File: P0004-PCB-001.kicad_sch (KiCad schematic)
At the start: 5 parts

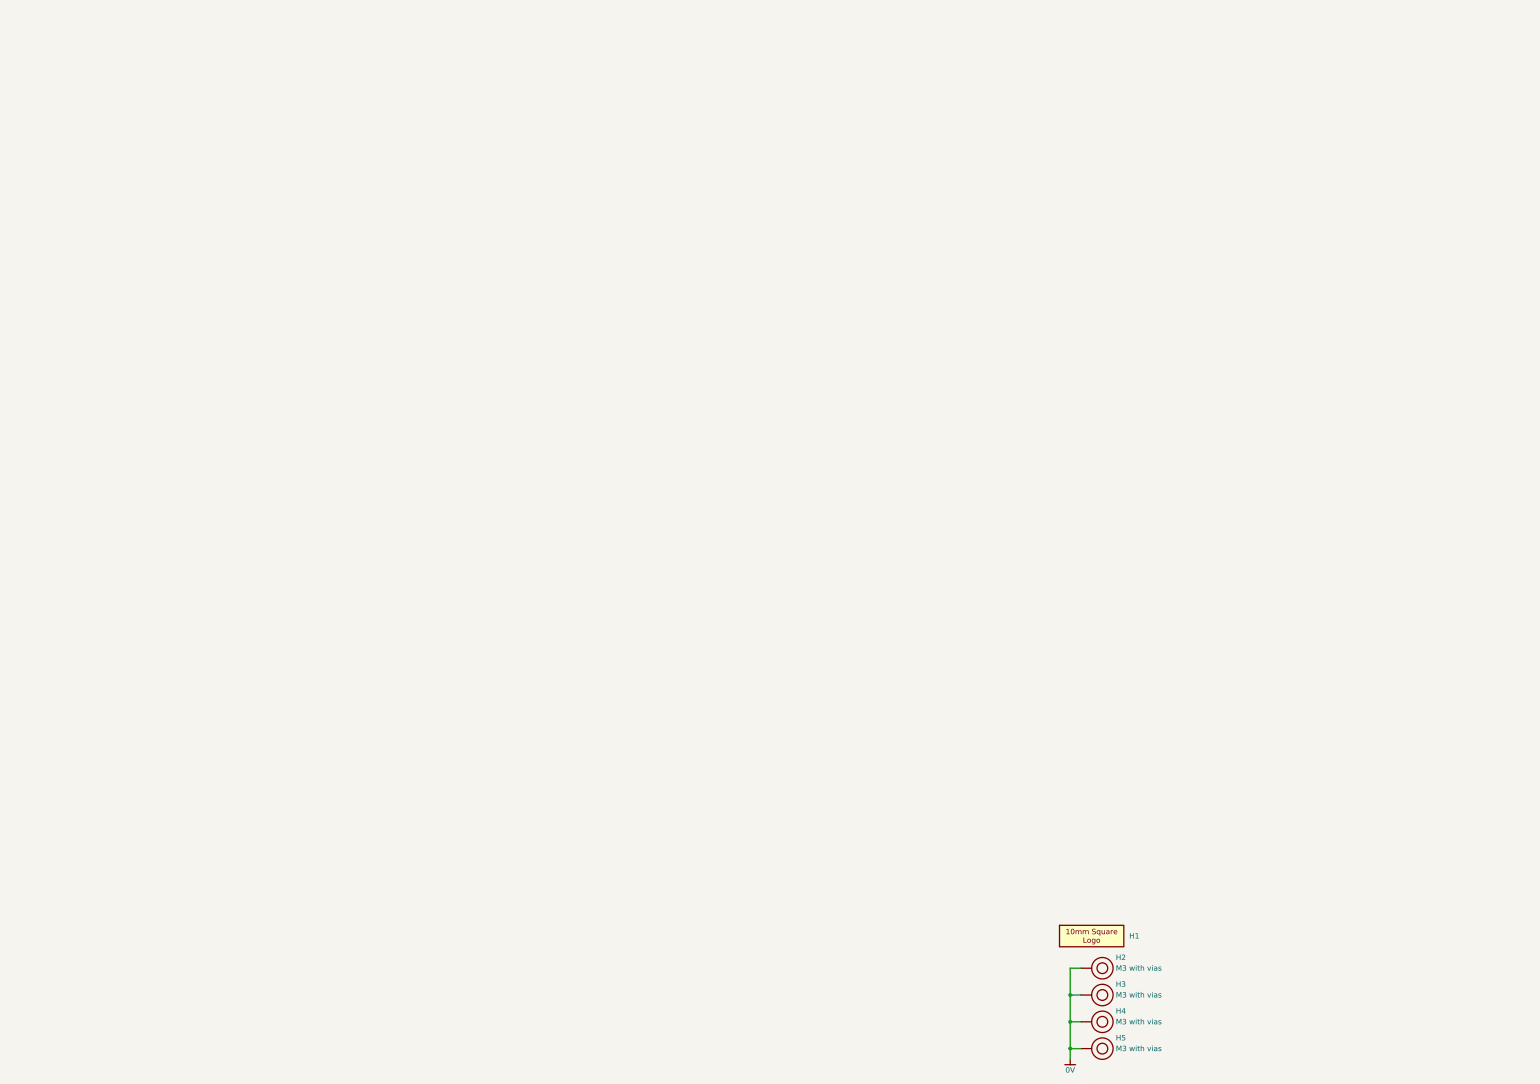
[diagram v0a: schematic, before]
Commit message: started adding components
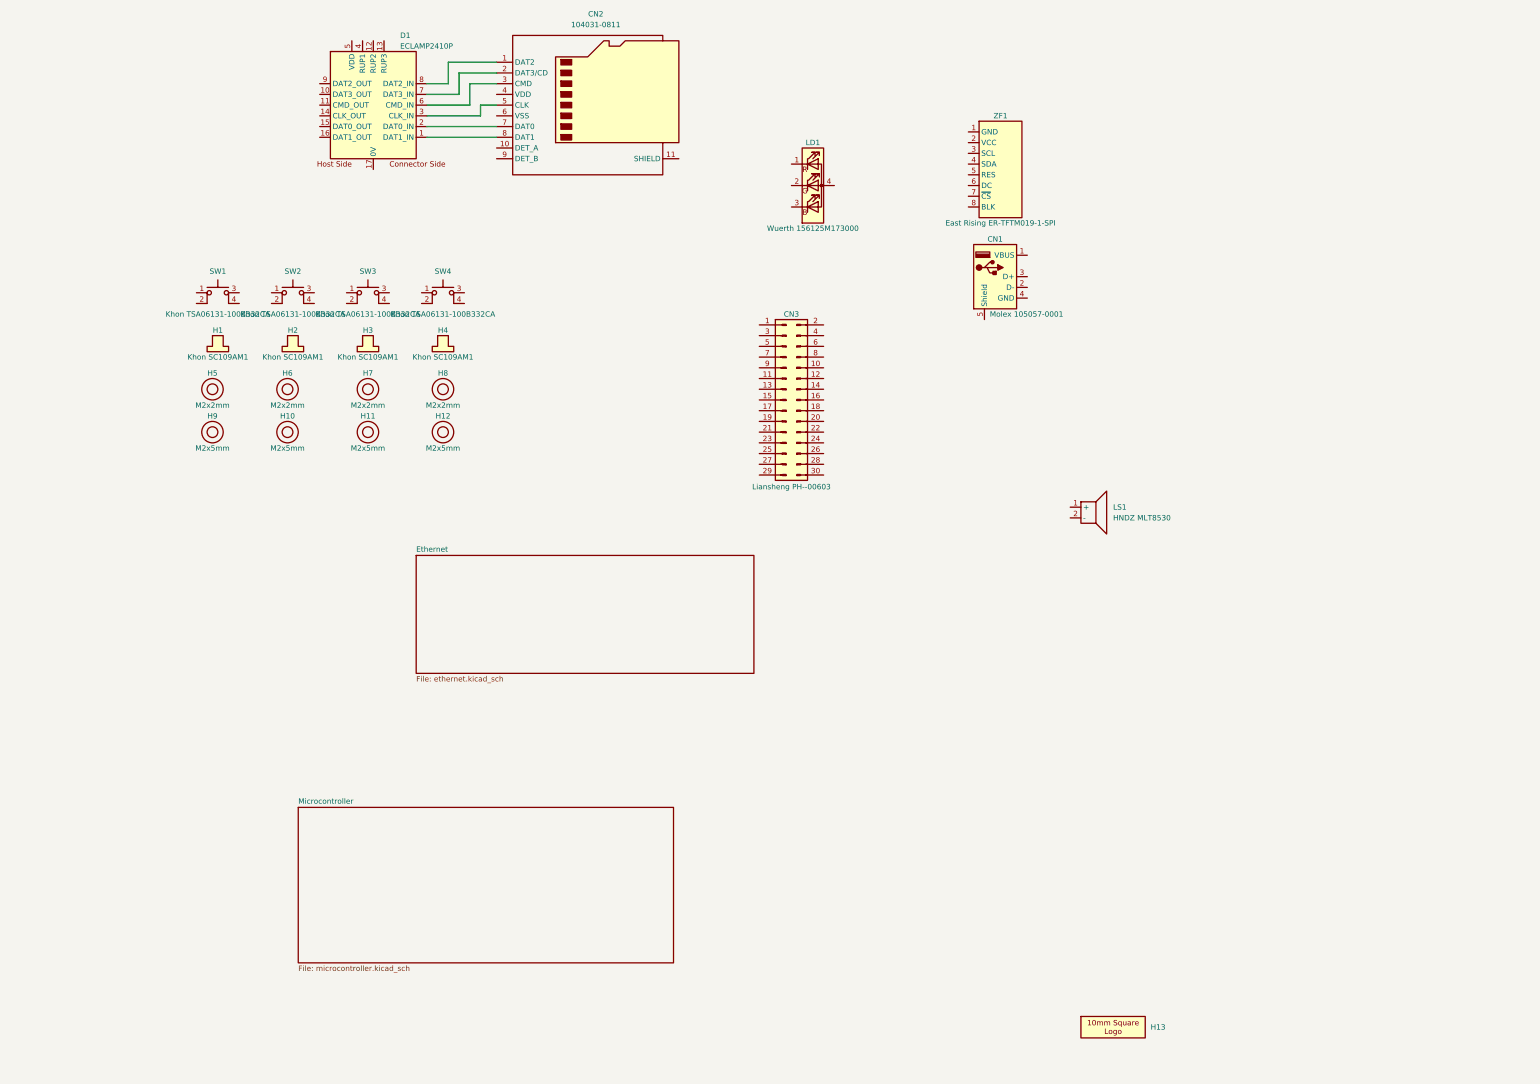
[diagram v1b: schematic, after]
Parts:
- removed H1: (no value), Misc_WUT:Logo_10mmx10mm, symbol Layout_WUT:Logo_10mmx10mm
- removed H2, H3, H4, H5: M3 with vias, MountingHole:MountingHole_3.2mm_M3_Pad_Via, symbol Layout_WUT:M3_with_Vias
- added CN1: Molex 105057-0001, Connector_WUT:USB-A_Molex_105057-0001_TH_Vertical, symbol Connector_WUT:Molex_105057-0001
- added CN2: 104031-0811, Connector_WUT:microSD_HC_Molex_104031-0811, symbol Connector_WUT:Molex_104031-0811
- added CN3: Liansheng PH--00603, Connector_WUT:Liansheng_PH--00603, symbol Connector_WUT:Liansheng_PH-00603
- added D1: ECLAMP2410P, Diode_WUT:Semtech_ECLAMP2410P, symbol Diode_WUT:Semtech_EClamp2410P
- added H1, H2, H3, H4: Khon SC109AM1, Switch_WUT:Khon_SC109, symbol Switch_WUT:Khon_SC109AM1
- added H10, H11, H12, H9: M2x5mm, Accessories_WUT:Accu_HPS-4-2.2-5-POM-BL, symbol Accessories_WUT:Accu_HPS-4-2.2-5-POM-BL
- added H13: (no value), Misc_WUT:Logo_10mmx10mm, symbol Layout_WUT:Logo_10mmx10mm
- added H5, H6, H7, H8: M2x2mm, Accessories_WUT:Accu_HPS-4-2.2-2-POM-BL, symbol Accessories_WUT:Accu_HPS-4-2.2-2-POM-BL
- added LD1: Wuerth 156125M173000, LED_WUT:Wuerth_156125M173000, symbol LED_WUT:Wuerth_156125M173000
- added LS1: HNDZ MLT8530, Audio_WUT:HNDZ_MLT8530, symbol Audio_WUT:HNDZ_MLT8530
- added SW1, SW2, SW3, SW4: Khon TSA06131-100B332CA, Switch_WUT:Khon_TSB06331-090, symbol Switch_WUT:Khon_TSB06331-090D332DA-R0500
- added ZF1: East Rising ER-TFTM019-1-SPI, Display_WUT:East-Rising_ER-TFTM019-1-SPI, symbol Display_WUT:East-Rising_ER-TFTM019-1-SPI
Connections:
- new net: LS1.3, LS1.4
- new net: CN2.8 (DAT1), D1.1 (DAT1_IN)
- new net: CN2.7 (DAT0), D1.2 (DAT0_IN)
- new net: CN2.5 (CLK), D1.3 (CLK_IN)
- new net: CN2.3 (CMD), D1.6 (CMD_IN)
- new net: CN2.2 (DAT3/CD), D1.7 (DAT3_IN)
- new net: CN2.1 (DAT2), D1.8 (DAT2_IN)
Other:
- added sheet Ethernet (ethernet.kicad_sch)
- added sheet Microcontroller (microcontroller.kicad_sch)

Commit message: testing ci config
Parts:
- SW1, SW2, SW3, SW4: value Khon TSA06131-100B332CA -> Khon TSB06331-090D332DA-R0500
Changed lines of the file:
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@@
 		(fields_autoplaced yes)
 		(property "Reference" "SW2"
+			(at 78.74 88.9 0)
+			(show_name no)
+			(do_not_autoplace no)
+			(effects
+				(font
+					(size 1.27 1.27)
+				)
+			)
+		)
+		(property "Value" "Khon TSB06331-090D332DA-R0500"
 			(at 78.74 91.44 0)
 			(show_name no)
 			(do_not_autoplace no)
-			(effects
-				(font
-					(size 1.27 1.27)
-				)
-			)
-		)
-		(property "Value" "Khon TSA06131-100B332CA"
-			(at 78.74 101.6 0)
-			(show_name no)
-			(do_not_autoplace yes)
 			(effects
 				(font
@@
 		(fields_autoplaced yes)
 		(property "Reference" "SW4"
+			(at 114.3 88.9 0)
+			(show_name no)
+			(do_not_autoplace no)
+			(effects
+				(font
+					(size 1.27 1.27)
+				)
+			)
+		)
+		(property "Value" "Khon TSB06331-090D332DA-R0500"
 			(at 114.3 91.44 0)
 			(show_name no)
 			(do_not_autoplace no)
-			(effects
-				(font
-					(size 1.27 1.27)
-				)
-			)
-		)
-		(property "Value" "Khon TSA06131-100B332CA"
-			(at 114.3 101.6 0)
-			(show_name no)
-			(do_not_autoplace yes)
 			(effects
 				(font
@@
 		(in_bom yes)
 		(on_board yes)
-		(in_pos_files yes)
+		(in_pos_files no)
 		(dnp no)
 		(fields_autoplaced yes)
@@
 		(in_bom yes)
 		(on_board yes)
-		(in_pos_files yes)
+		(in_pos_files no)
 		(dnp no)
 		(fields_autoplaced yes)
@@
 		(fields_autoplaced yes)
 		(property "Reference" "SW1"
+			(at 60.96 88.9 0)
+			(show_name no)
+			(do_not_autoplace no)
+			(effects
+				(font
+					(size 1.27 1.27)
+				)
+			)
+		)
+		(property "Value" "Khon TSB06331-090D332DA-R0500"
 			(at 60.96 91.44 0)
 			(show_name no)
 			(do_not_autoplace no)
-			(effects
-				(font
-					(size 1.27 1.27)
-				)
-			)
-		)
-		(property "Value" "Khon TSA06131-100B332CA"
-			(at 60.96 101.6 0)
-			(show_name no)
-			(do_not_autoplace yes)
 			(effects
 				(font
@@
 		(in_bom yes)
 		(on_board yes)
-		(in_pos_files yes)
+		(in_pos_files no)
 		(dnp no)
 		(fields_autoplaced yes)
@@
 		(fields_autoplaced yes)
 		(property "Reference" "SW3"
+			(at 96.52 88.9 0)
+			(show_name no)
+			(do_not_autoplace no)
+			(effects
+				(font
+					(size 1.27 1.27)
+				)
+			)
+		)
+		(property "Value" "Khon TSB06331-090D332DA-R0500"
 			(at 96.52 91.44 0)
 			(show_name no)
 			(do_not_autoplace no)
-			(effects
-				(font
-					(size 1.27 1.27)
-				)
-			)
-		)
-		(property "Value" "Khon TSA06131-100B332CA"
-			(at 96.52 101.6 0)
-			(show_name no)
-			(do_not_autoplace yes)
 			(effects
 				(font
@@
 		(in_bom yes)
 		(on_board yes)
-		(in_pos_files yes)
+		(in_pos_files no)
 		(dnp no)
 		(fields_autoplaced yes)

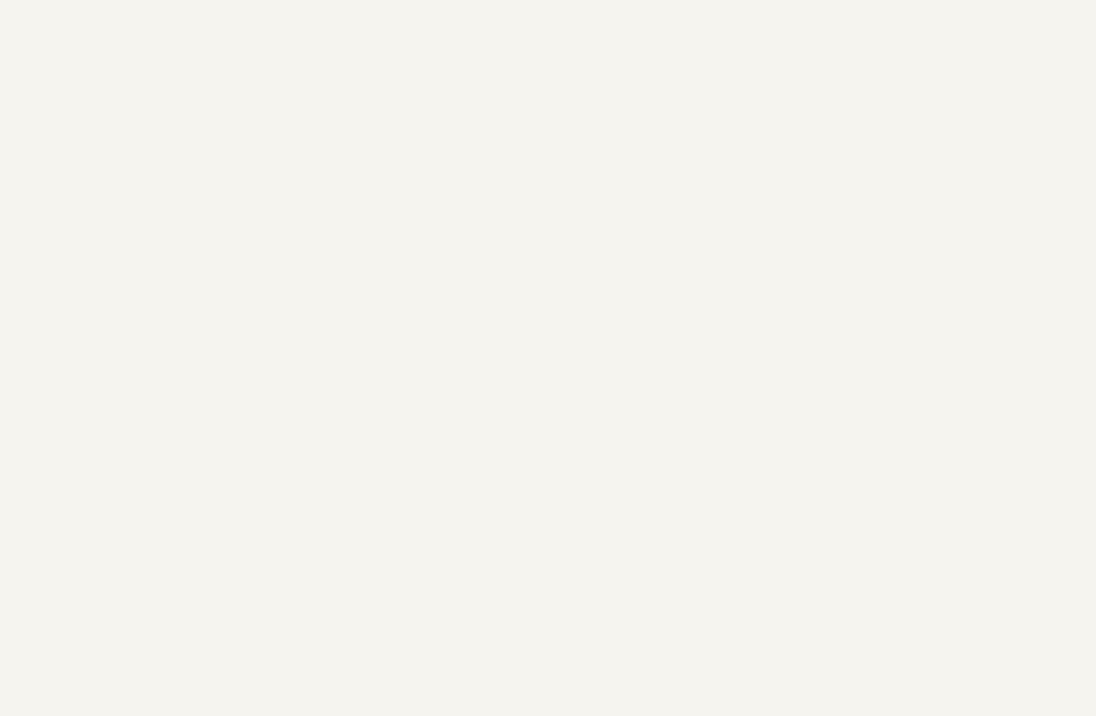
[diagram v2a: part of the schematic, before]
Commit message: started on DCDC section
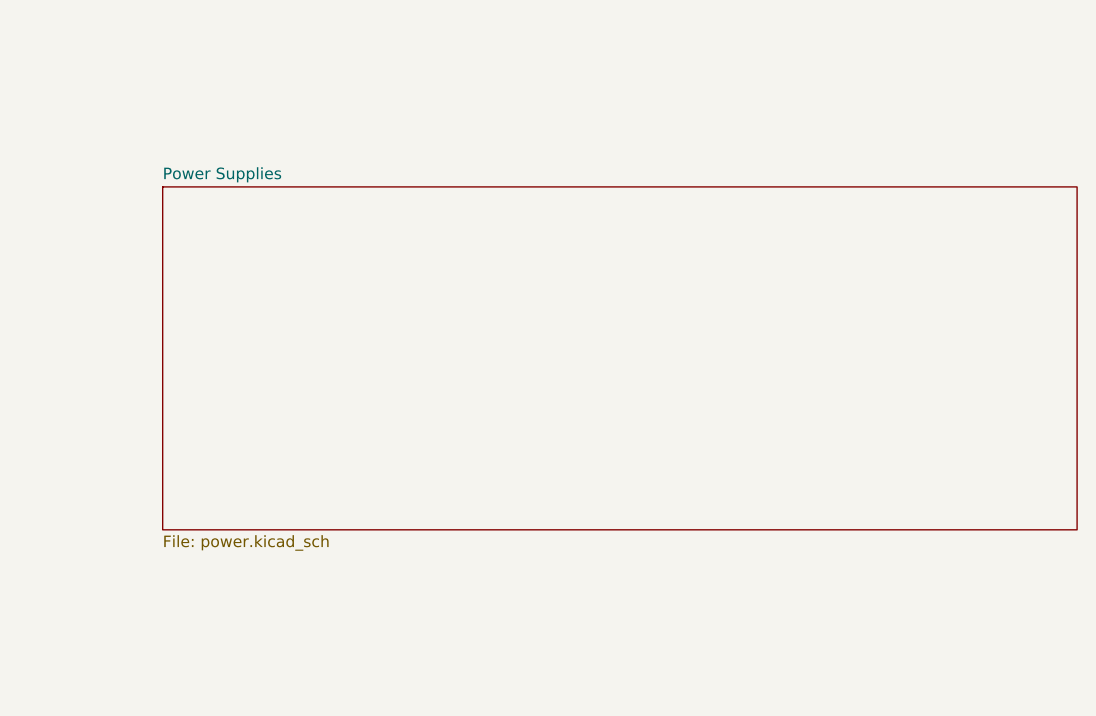
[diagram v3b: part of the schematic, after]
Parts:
- H1, H2, H3, H4: JLCPCB Order # (none) -> C42435457; MPN (none) -> SC109AM1; Manufacturer (none) -> Khon
- LD1: JLCPCB Order # (none) -> C5341671; MPN https://www.we-online.com/components/products/datasheet/156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 -> 156125M173000
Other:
- added sheet Power Supplies (power.kicad_sch)
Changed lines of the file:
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@@
 			)
 		)
-		(property "Datasheet" ""
+		(property "Datasheet" "https://www.khon-switch.com/upload/1c/202307/SC109%20Switch%20Cap.pdf"
 			(at 60.96 109.22 0)
 			(hide yes)
@@
 			)
 		)
-		(property "Description" ""
+		(property "Description" "Switch cap"
+			(at 60.96 109.22 0)
+			(hide yes)
+			(show_name no)
+			(do_not_autoplace no)
+			(effects
+				(font
+					(size 1.27 1.27)
+				)
+			)
+		)
+		(property "Manufacturer" "Khon"
+			(at 60.96 109.22 0)
+			(hide yes)
+			(show_name no)
+			(do_not_autoplace no)
+			(effects
+				(font
+					(size 1.27 1.27)
+				)
+			)
+		)
+		(property "MPN" "SC109AM1"
+			(at 60.96 109.22 0)
+			(hide yes)
+			(show_name no)
+			(do_not_autoplace no)
+			(effects
+				(font
+					(size 1.27 1.27)
+				)
+			)
+		)
+		(property "JLCPCB Order #" "C42435457"
 			(at 60.96 109.22 0)
 			(hide yes)
@@
 			)
 		)
-		(property "Datasheet" ""
+		(property "Datasheet" "https://www.khon-switch.com/upload/1c/202307/SC109%20Switch%20Cap.pdf"
 			(at 78.74 109.22 0)
 			(hide yes)
@@
 			)
 		)
-		(property "Description" ""
+		(property "Description" "Switch cap"
+			(at 78.74 109.22 0)
+			(hide yes)
+			(show_name no)
+			(do_not_autoplace no)
+			(effects
+				(font
+					(size 1.27 1.27)
+				)
+			)
+		)
+		(property "Manufacturer" "Khon"
+			(at 78.74 109.22 0)
+			(hide yes)
+			(show_name no)
+			(do_not_autoplace no)
+			(effects
+				(font
+					(size 1.27 1.27)
+				)
+			)
+		)
+		(property "MPN" "SC109AM1"
+			(at 78.74 109.22 0)
+			(hide yes)
+			(show_name no)
+			(do_not_autoplace no)
+			(effects
+				(font
+					(size 1.27 1.27)
+				)
+			)
+		)
+		(property "JLCPCB Order #" "C42435457"
 			(at 78.74 109.22 0)
 			(hide yes)
@@
 			)
 		)
-		(property "MPN" "https://www.we-online.com/components/products/datasheet/156125M173000.pdf"
+		(property "MPN" "156125M173000"
+			(at 201.93 71.12 0)
+			(hide yes)
+			(show_name no)
+			(do_not_autoplace no)
+			(effects
+				(font
+					(size 1.27 1.27)
+				)
+			)
+		)
+		(property "JLCPCB Order #" "C5341671"
 			(at 201.93 71.12 0)
 			(hide yes)
@@
 			)
 		)
-		(property "Datasheet" ""
+		(property "Datasheet" "https://www.khon-switch.com/upload/1c/202307/SC109%20Switch%20Cap.pdf"
 			(at 114.3 109.22 0)
 			(hide yes)
@@
 			)
 		)
-		(property "Description" ""
+		(property "Description" "Switch cap"
+			(at 114.3 109.22 0)
+			(hide yes)
+			(show_name no)
+			(do_not_autoplace no)
+			(effects
+				(font
+					(size 1.27 1.27)
+				)
+			)
+		)
+		(property "Manufacturer" "Khon"
+			(at 114.3 109.22 0)
+			(hide yes)
+			(show_name no)
+			(do_not_autoplace no)
+			(effects
+				(font
+					(size 1.27 1.27)
+				)
+			)
+		)
+		(property "MPN" "SC109AM1"
+			(at 114.3 109.22 0)
+			(hide yes)
+			(show_name no)
+			(do_not_autoplace no)
+			(effects
+				(font
+					(size 1.27 1.27)
+				)
+			)
+		)
+		(property "JLCPCB Order #" "C42435457"
 			(at 114.3 109.22 0)
 			(hide yes)
@@
 			)
 		)
-		(property "Datasheet" ""
+		(property "Datasheet" "https://www.khon-switch.com/upload/1c/202307/SC109%20Switch%20Cap.pdf"
 			(at 96.52 109.22 0)
 			(hide yes)
@@
 			)
 		)
-		(property "Description" ""
+		(property "Description" "Switch cap"
+			(at 96.52 109.22 0)
+			(hide yes)
+			(show_name no)
+			(do_not_autoplace no)
+			(effects
+				(font
+					(size 1.27 1.27)
+				)
+			)
+		)
+		(property "Manufacturer" "Khon"
+			(at 96.52 109.22 0)
+			(hide yes)
+			(show_name no)
+			(do_not_autoplace no)
+			(effects
+				(font
+					(size 1.27 1.27)
+				)
+			)
+		)
+		(property "MPN" "SC109AM1"
+			(at 96.52 109.22 0)
+			(hide yes)
+			(show_name no)
+			(do_not_autoplace no)
+			(effects
+				(font
+					(size 1.27 1.27)
+				)
+			)
+		)
+		(property "JLCPCB Order #" "C42435457"
 			(at 96.52 109.22 0)
 			(hide yes)
@@
 				)
 			)
+		)
+	)
+	(sheet
+		(at 267.97 179.07)
+		(size 101.6 38.1)
+		(exclude_from_sim no)
+		(in_bom yes)
+		(on_board yes)
+		(dnp no)
+		(fields_autoplaced yes)
+		(stroke
+			(width 0.1524)
+			(type solid)
+		)
+		(fill
+			(color 0 0 0 0)
+		)
+		(property "Sheetname" "Power Supplies"
+			(at 267.97 178.3584 0)
+			(show_name no)
+			(do_not_autoplace no)
+			(effects
+				(font
+					(size 1.27 1.27)
+				)
+				(justify left bottom)
+			)
+		)
+		(property "Sheetfile" "power.kicad_sch"
+			(at 267.97 217.7546 0)
+			(show_name no)
+			(do_not_autoplace no)
+			(effects
+				(font
+					(size 1.27 1.27)
+				)
+				(justify left top)
+			)
+		)
+		(instances
+			(project "P0004-PCB-001"
+				(path "/acdb93e6-9aa6-4a78-8a68-9d0ae3318f45"
+					(page "4")
+				)
+			)
